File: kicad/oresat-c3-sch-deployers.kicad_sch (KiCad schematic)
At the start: 20 parts, among them Q10 FDMQ86530L, Q11 DMP2240UDM-7, Q5 DMP2240UDM-7, Q7 DMP2240UDM-7, Q8 FDMQ86530L, Q9 DMP2240UDM-7

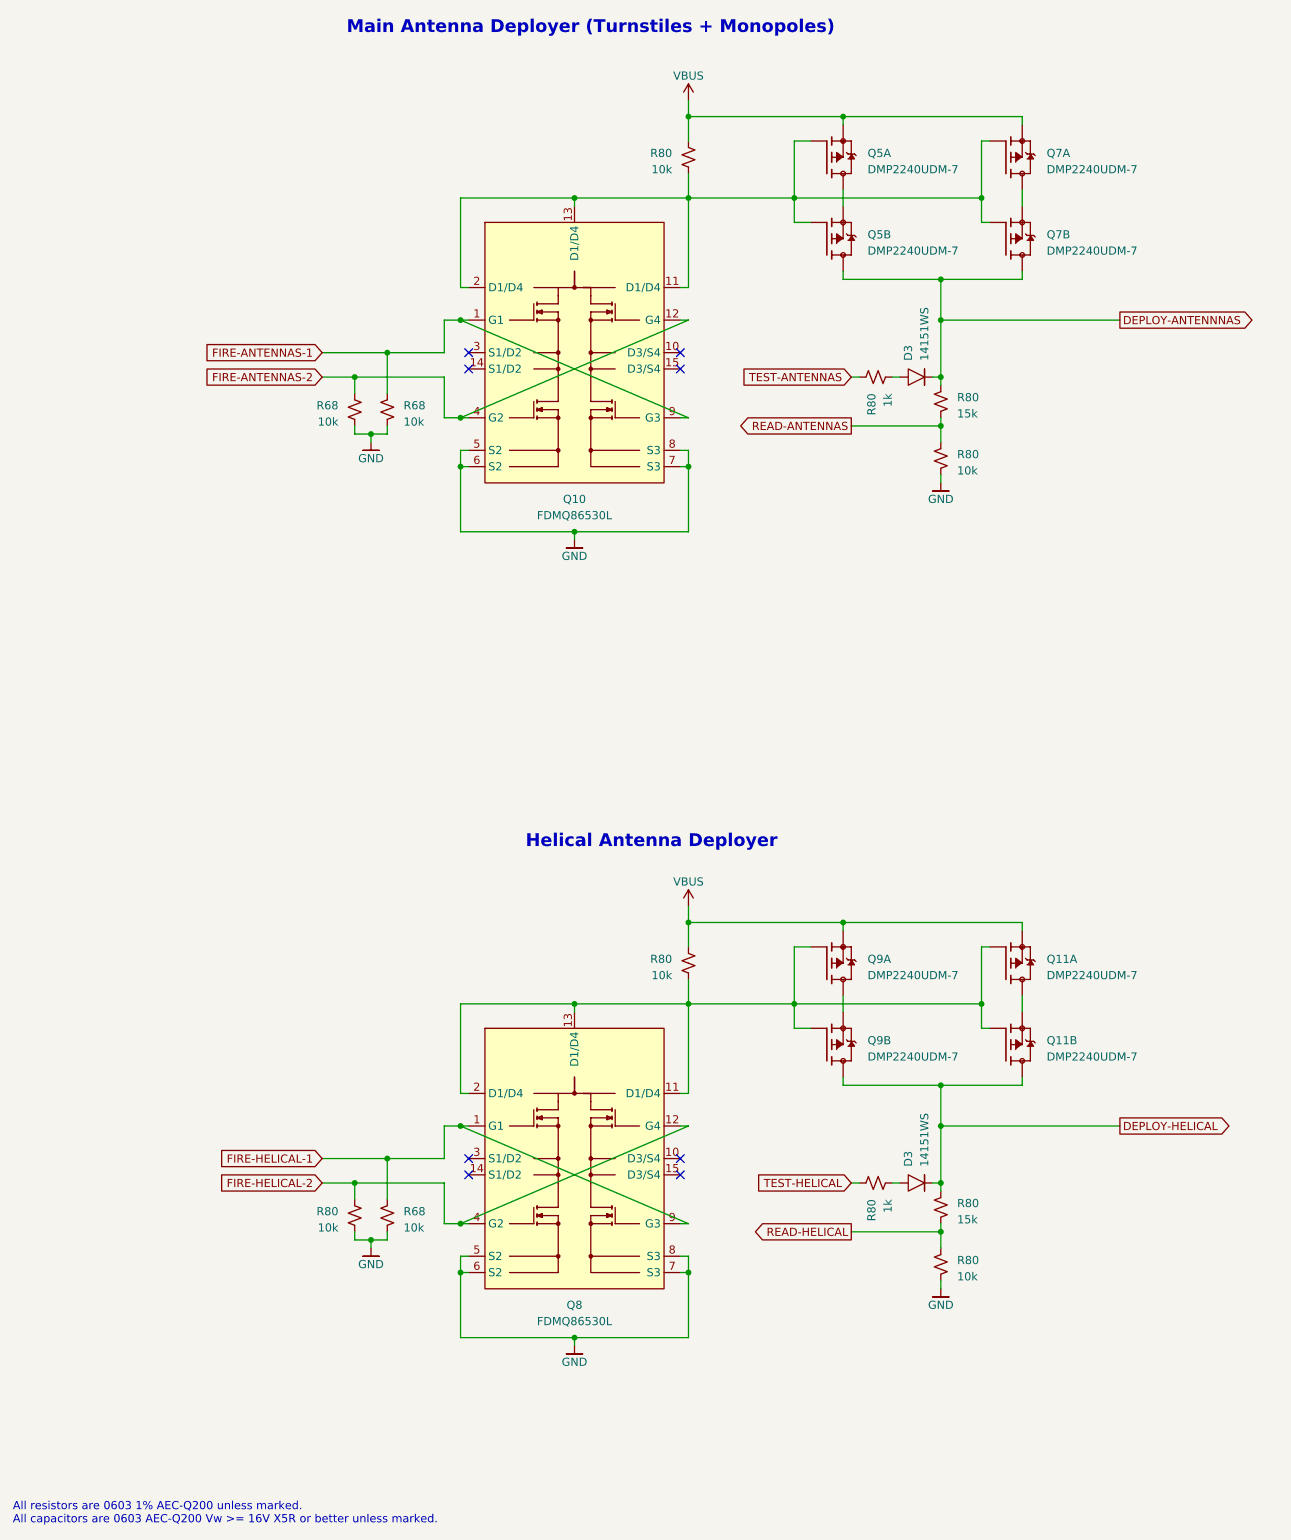
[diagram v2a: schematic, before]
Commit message: Big C3 cleanup with Glenn; radios off of one SPS + separate LDOs, removed lots of test 0 ohm resistors, cleaned up capacitance, and finally wired everything up to the octavo. ZERO ERC errors.
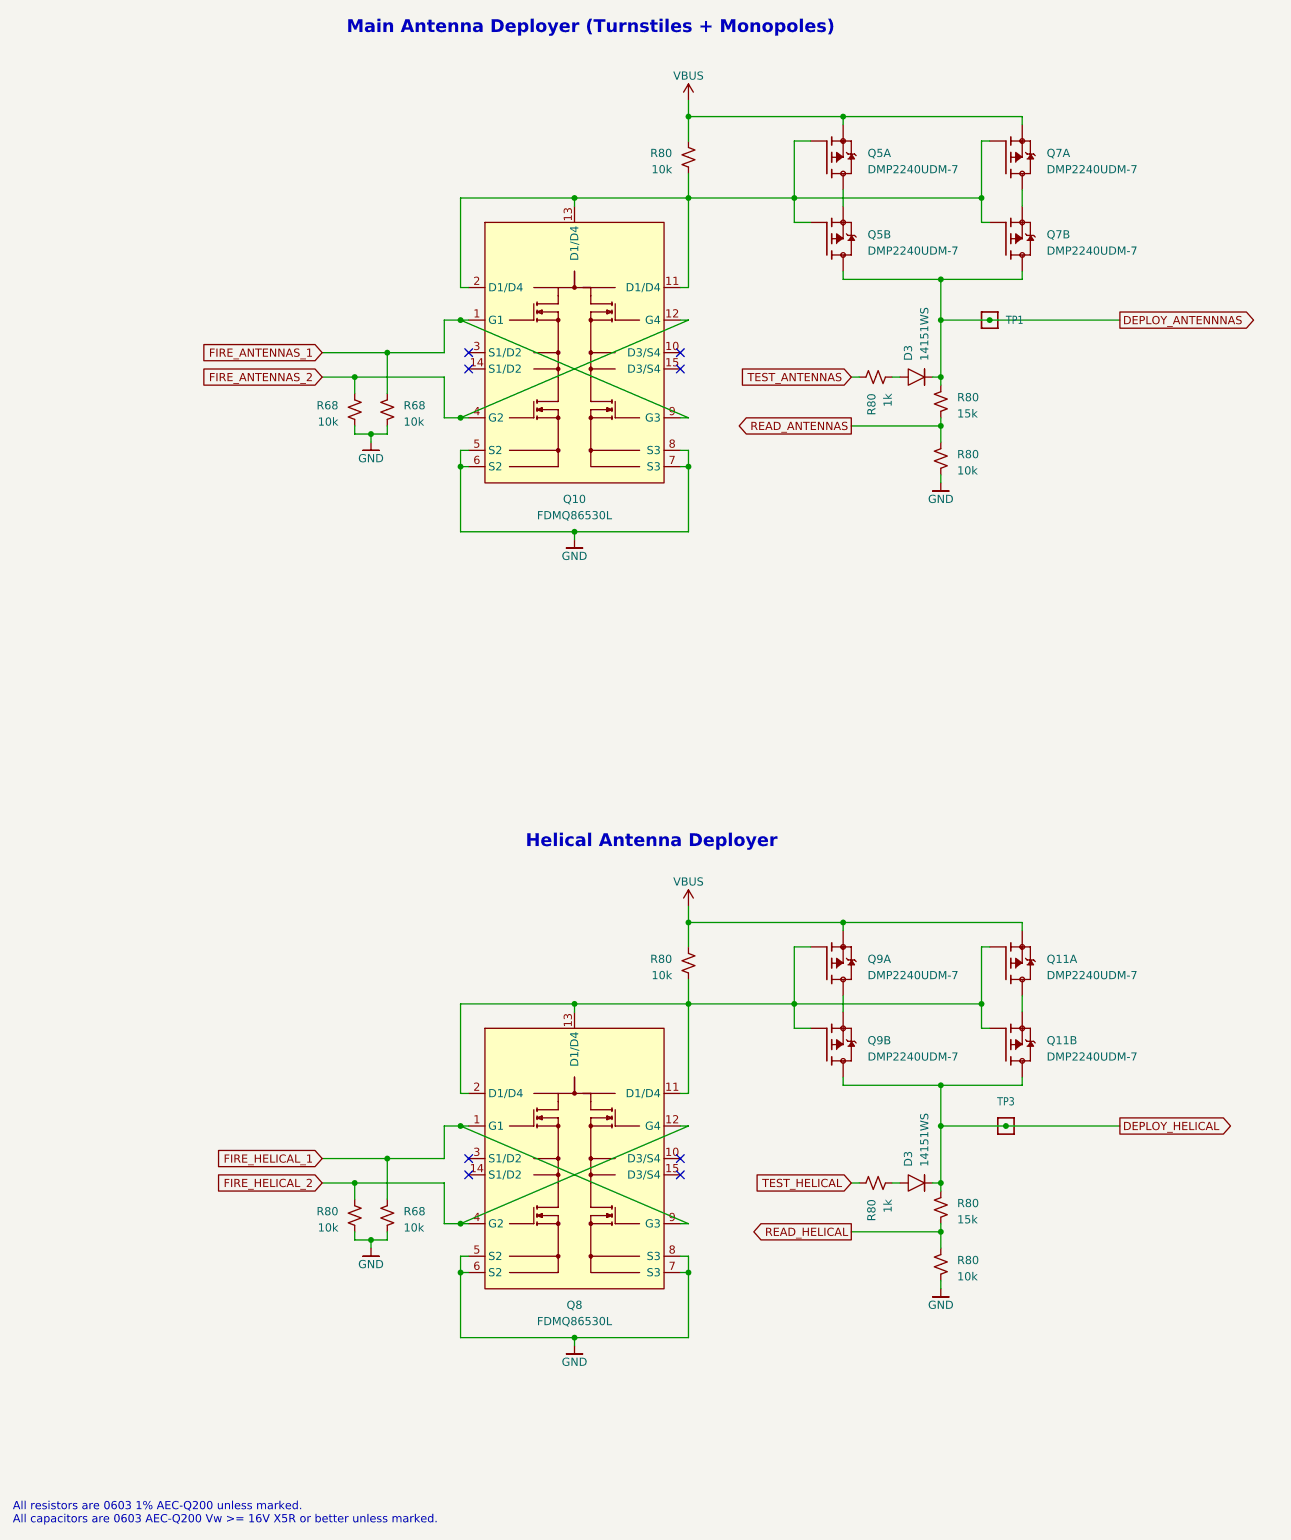
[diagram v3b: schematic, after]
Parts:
- added TP1, TP3: Test-Point, TestPoint:TestPoint_Pad_D1.0mm, symbol oresat-misc:Test-Point-1mm-round
- Q10, Q8: footprint oresat-c3:FDMQ8203 -> oresat-transistors:FDMQ86530L
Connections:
- net DEPLOY-ANTENNNAS renamed DEPLOY_ANTENNNAS
- net DEPLOY_ANTENNNAS: now also TP1.1
- net DEPLOY-HELICAL renamed DEPLOY_HELICAL
- net DEPLOY_HELICAL: now also TP3.1
- net FIRE-ANTENNAS-1 renamed FIRE_ANTENNAS_1
- net FIRE-ANTENNAS-2 renamed FIRE_ANTENNAS_2
- net FIRE-HELICAL-1 renamed FIRE_HELICAL_1
- net FIRE-HELICAL-2 renamed FIRE_HELICAL_2
- net READ-ANTENNAS renamed READ_ANTENNAS
- net READ-HELICAL renamed READ_HELICAL
- net TEST-ANTENNAS renamed TEST_ANTENNAS
- net TEST-HELICAL renamed TEST_HELICAL
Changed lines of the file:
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@@
   (junction (at 220.98 54.61) (diameter 0) (color 0 0 0 0)
   )
+  (junction (at 267.97 73.66) (diameter 0) (color 0 0 0 0)
+  )
   (junction (at 260.35 215.9) (diameter 0) (color 0 0 0 0)
   )
@@
   )
   (junction (at 260.35 208.28) (diameter 0) (color 0 0 0 0)
+  )
+  (junction (at 270.51 199.39) (diameter 0) (color 0 0 0 0)
   )
   (junction (at 185.42 222.25) (diameter 0) (color 0 0 0 0)
@@
     (stroke (width 0) (type default))
   )
+  (wire (pts (xy 270.51 199.39) (xy 260.35 199.39))
+    (stroke (width 0) (type default))
+  )
   (wire (pts (xy 220.98 199.39) (xy 219.71 199.39))
     (stroke (width 0) (type default))
@@
     (stroke (width 0) (type default))
   )
+  (wire (pts (xy 267.97 73.66) (xy 260.35 73.66))
+    (stroke (width 0) (type default))
+  )
   (wire (pts (xy 260.35 224.79) (xy 260.35 223.52))
     (stroke (width 0) (type default))
@@
     (stroke (width 0) (type default))
   )
-  (wire (pts (xy 288.29 73.66) (xy 260.35 73.66))
+  (wire (pts (xy 288.29 73.66) (xy 267.97 73.66))
     (stroke (width 0) (type default))
   )
@@
     (stroke (width 0) (type default))
   )
-  (wire (pts (xy 288.29 199.39) (xy 260.35 199.39))
+  (wire (pts (xy 288.29 199.39) (xy 270.51 199.39))
     (stroke (width 0) (type default))
   )
@@
     (effects (font (size 2 2) (thickness 0.4) bold) (justify left bottom))
   )
-  (global_label "FIRE-HELICAL-2" (shape input) (at 163.83 208.28 180) (fields_autoplaced)
+  (global_label "FIRE_HELICAL_2" (shape input) (at 163.83 208.28 180) (fields_autoplaced)
     (effects (font (size 1.27 1.27)) (justify right))
-    (property "Intersheetrefs" "${INTERSHEET_REFS}" (at 144.9584 208.28 0)
-      (effects (font (size 1.27 1.27)) (justify right))
-    )
-  )
-  (global_label "READ-HELICAL" (shape output) (at 246.38 215.9 180) (fields_autoplaced)
+    (property "Intersheetrefs" "${INTERSHEET_REFS}" (at 146.168 208.28 0)
+      (effects (font (size 1.27 1.27)) (justify right))
+    )
+  )
+  (global_label "READ_HELICAL" (shape output) (at 246.38 215.9 180) (fields_autoplaced)
     (effects (font (size 1.27 1.27)) (justify right))
-    (property "Intersheetrefs" "${INTERSHEET_REFS}" (at 229.6251 215.9 0)
-      (effects (font (size 1.27 1.27)) (justify right))
-    )
-  )
-  (global_label "DEPLOY-ANTENNNAS" (shape output) (at 288.29 73.66 0) (fields_autoplaced)
+    (property "Intersheetrefs" "${INTERSHEET_REFS}" (at 230.2299 215.9 0)
+      (effects (font (size 1.27 1.27)) (justify right))
+    )
+  )
+  (global_label "DEPLOY_ANTENNNAS" (shape output) (at 288.29 73.66 0) (fields_autoplaced)
     (effects (font (size 1.27 1.27)) (justify left))
-    (property "Intersheetrefs" "${INTERSHEET_REFS}" (at 310.7297 73.66 0)
-      (effects (font (size 1.27 1.27)) (justify left))
-    )
-  )
-  (global_label "FIRE-ANTENNAS-2" (shape input) (at 163.83 82.55 180) (fields_autoplaced)
+    (property "Intersheetrefs" "${INTERSHEET_REFS}" (at 310.1249 73.66 0)
+      (effects (font (size 1.27 1.27)) (justify left))
+    )
+  )
+  (global_label "FIRE_ANTENNAS_2" (shape input) (at 163.83 82.55 180) (fields_autoplaced)
     (effects (font (size 1.27 1.27)) (justify right))
-    (property "Intersheetrefs" "${INTERSHEET_REFS}" (at 142.9627 82.55 0)
-      (effects (font (size 1.27 1.27)) (justify right))
-    )
-  )
-  (global_label "READ-ANTENNAS" (shape output) (at 246.38 90.17 180) (fields_autoplaced)
+    (property "Intersheetrefs" "${INTERSHEET_REFS}" (at 144.1723 82.55 0)
+      (effects (font (size 1.27 1.27)) (justify right))
+    )
+  )
+  (global_label "READ_ANTENNAS" (shape output) (at 246.38 90.17 180) (fields_autoplaced)
     (effects (font (size 1.27 1.27)) (justify right))
-    (property "Intersheetrefs" "${INTERSHEET_REFS}" (at 227.6294 90.17 0)
-      (effects (font (size 1.27 1.27)) (justify right))
-    )
-  )
-  (global_label "FIRE-ANTENNAS-1" (shape input) (at 163.83 78.74 180) (fields_autoplaced)
+    (property "Intersheetrefs" "${INTERSHEET_REFS}" (at 228.2342 90.17 0)
+      (effects (font (size 1.27 1.27)) (justify right))
+    )
+  )
+  (global_label "FIRE_ANTENNAS_1" (shape input) (at 163.83 78.74 180) (fields_autoplaced)
     (effects (font (size 1.27 1.27)) (justify right))
-    (property "Intersheetrefs" "${INTERSHEET_REFS}" (at 142.9627 78.74 0)
-      (effects (font (size 1.27 1.27)) (justify right))
-    )
-  )
-  (global_label "TEST-HELICAL" (shape input) (at 246.38 208.28 180) (fields_autoplaced)
+    (property "Intersheetrefs" "${INTERSHEET_REFS}" (at 144.1723 78.74 0)
+      (effects (font (size 1.27 1.27)) (justify right))
+    )
+  )
+  (global_label "TEST_HELICAL" (shape input) (at 246.38 208.28 180) (fields_autoplaced)
     (effects (font (size 1.27 1.27)) (justify right))
-    (property "Intersheetrefs" "${INTERSHEET_REFS}" (at 230.109 208.28 0)
-      (effects (font (size 1.27 1.27)) (justify right))
-    )
-  )
-  (global_label "DEPLOY-HELICAL" (shape output) (at 288.29 199.39 0) (fields_autoplaced)
+    (property "Intersheetrefs" "${INTERSHEET_REFS}" (at 230.7138 208.28 0)
+      (effects (font (size 1.27 1.27)) (justify right))
+    )
+  )
+  (global_label "DEPLOY_HELICAL" (shape output) (at 288.29 199.39 0) (fields_autoplaced)
     (effects (font (size 1.27 1.27)) (justify left))
-    (property "Intersheetrefs" "${INTERSHEET_REFS}" (at 307.4035 199.39 0)
-      (effects (font (size 1.27 1.27)) (justify left))
-    )
-  )
-  (global_label "TEST-ANTENNAS" (shape input) (at 246.38 82.55 180) (fields_autoplaced)
+    (property "Intersheetrefs" "${INTERSHEET_REFS}" (at 306.7987 199.39 0)
+      (effects (font (size 1.27 1.27)) (justify left))
+    )
+  )
+  (global_label "TEST_ANTENNAS" (shape input) (at 246.38 82.55 180) (fields_autoplaced)
     (effects (font (size 1.27 1.27)) (justify right))
-    (property "Intersheetrefs" "${INTERSHEET_REFS}" (at 228.1133 82.55 0)
-      (effects (font (size 1.27 1.27)) (justify right))
-    )
-  )
-  (global_label "FIRE-HELICAL-1" (shape input) (at 163.83 204.47 180) (fields_autoplaced)
+    (property "Intersheetrefs" "${INTERSHEET_REFS}" (at 228.7181 82.55 0)
+      (effects (font (size 1.27 1.27)) (justify right))
+    )
+  )
+  (global_label "FIRE_HELICAL_1" (shape input) (at 163.83 204.47 180) (fields_autoplaced)
     (effects (font (size 1.27 1.27)) (justify right))
-    (property "Intersheetrefs" "${INTERSHEET_REFS}" (at 144.9584 204.47 0)
-      (effects (font (size 1.27 1.27)) (justify right))
+    (property "Intersheetrefs" "${INTERSHEET_REFS}" (at 146.168 204.47 0)
+      (effects (font (size 1.27 1.27)) (justify right))
+    )
+  )
+  (symbol (lib_id "oresat-misc:Test-Point-1mm-round") (at 270.51 199.39 180) (unit 1)
+    (in_bom yes) (on_board yes) (dnp no) (fields_autoplaced)
+    (property "Reference" "TP3" (at 270.51 195.58 0)
+      (effects (font (size 1.27 1.0795)))
+    )
+    (property "Value" "Test-Point" (at 270.51 207.01 0)
+      (effects (font (size 1.27 1.27)) hide)
+    )
+    (property "Footprint" "TestPoint:TestPoint_Pad_D1.0mm" (at 270.51 209.55 0)
+      (effects (font (size 1.27 1.27)) hide)
+    )
+    (property "Datasheet" "" (at 270.51 199.39 0)
+      (effects (font (size 1.27 1.27)) hide)
+    )
+    (pin "1")
+    (instances
+      (project "oresat-c3"
+        (path "/65d12cdd-c326-4033-9053-c59fa4e0b25e/f40986af-661f-42e2-86b8-cadc1b813505"
+          (reference "TP3") (unit 1)
+        )
+      )
     )
   )
@@
       (effects (font (size 1.27 1.27)))
     )
-    (property "Footprint" "oresat-c3:FDMQ8203" (at 203.2 45.72 0)
+    (property "Footprint" "oresat-transistors:FDMQ86530L" (at 203.2 45.72 0)
       (effects (font (size 1.27 1.27)) hide)
     )
@@
       (effects (font (size 1.27 1.27)))
     )
-    (property "Footprint" "oresat-c3:FDMQ8203" (at 203.2 171.45 0)
+    (property "Footprint" "oresat-transistors:FDMQ86530L" (at 203.2 171.45 0)
       (effects (font (size 1.27 1.27)) hide)
     )
@@
         )
       )
+    )
+  )
+  (symbol (lib_id "oresat-misc:Test-Point-1mm-round") (at 267.97 73.66 270) (unit 1)
+    (in_bom yes) (on_board yes) (dnp no) (fields_autoplaced)
+    (property "Reference" "TP1" (at 270.51 73.66 90)
+      (effects (font (size 1.27 1.0795)) (justify left))
+    )
+    (property "Value" "Test-Point" (at 275.59 73.66 0)
+      (effects (font (size 1.27 1.27)) hide)
+    )
+    (property "Footprint" "TestPoint:TestPoint_Pad_D1.0mm" (at 278.13 73.66 0)
+      (effects (font (size 1.27 1.27)) hide)
+    )
+    (property "Datasheet" "" (at 267.97 73.66 0)
+      (effects (font (size 1.27 1.27)) hide)
+    )
+    (pin "1")
+    (instances
+      (project "oresat-c3"
+        (path "/65d12cdd-c326-4033-9053-c59fa4e0b25e/f40986af-661f-42e2-86b8-cadc1b813505"
+          (reference "TP1") (unit 1)
+        )
+      )
